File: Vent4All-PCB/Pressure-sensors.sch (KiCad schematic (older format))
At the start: 4 parts, among them U2 HSCMRRN100MDSA3, U3 HSCMRRN100MDSA3, U4 HSCMRRN100MDSA3, U5 HSCMRRN100MDSA3

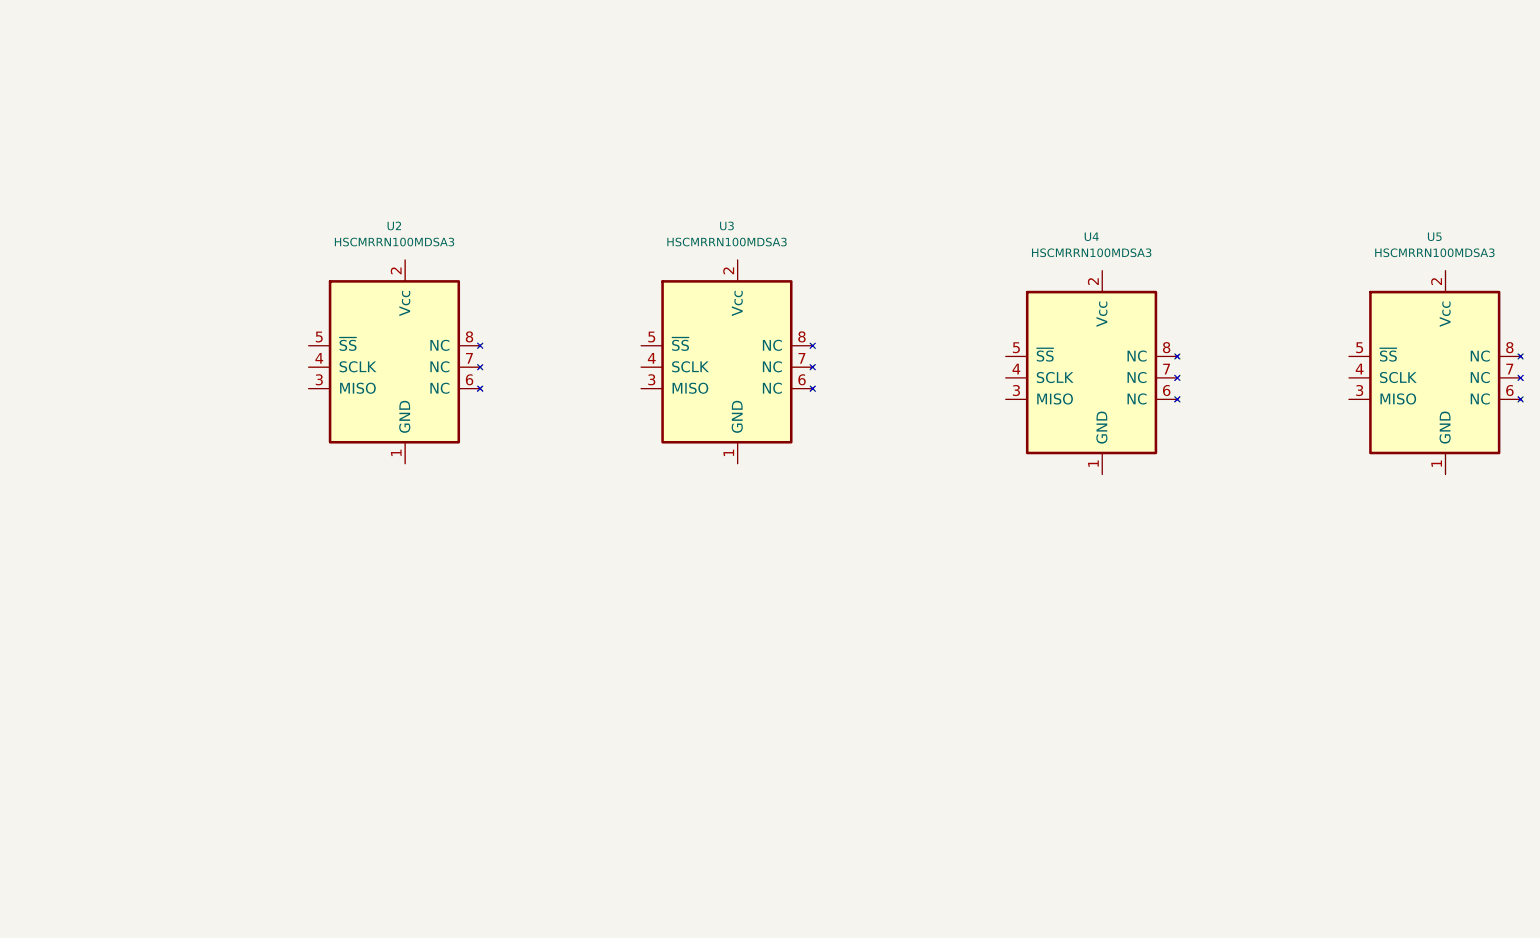
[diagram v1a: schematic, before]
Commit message: Added schematic connections for HSC sensors.
Note: this assumes HSC sensors will be soldered directly to the PCB. If we are placing them on daughter boards then we will need to choose the pin header connectors and move the HSC symbols into a separate sheet.
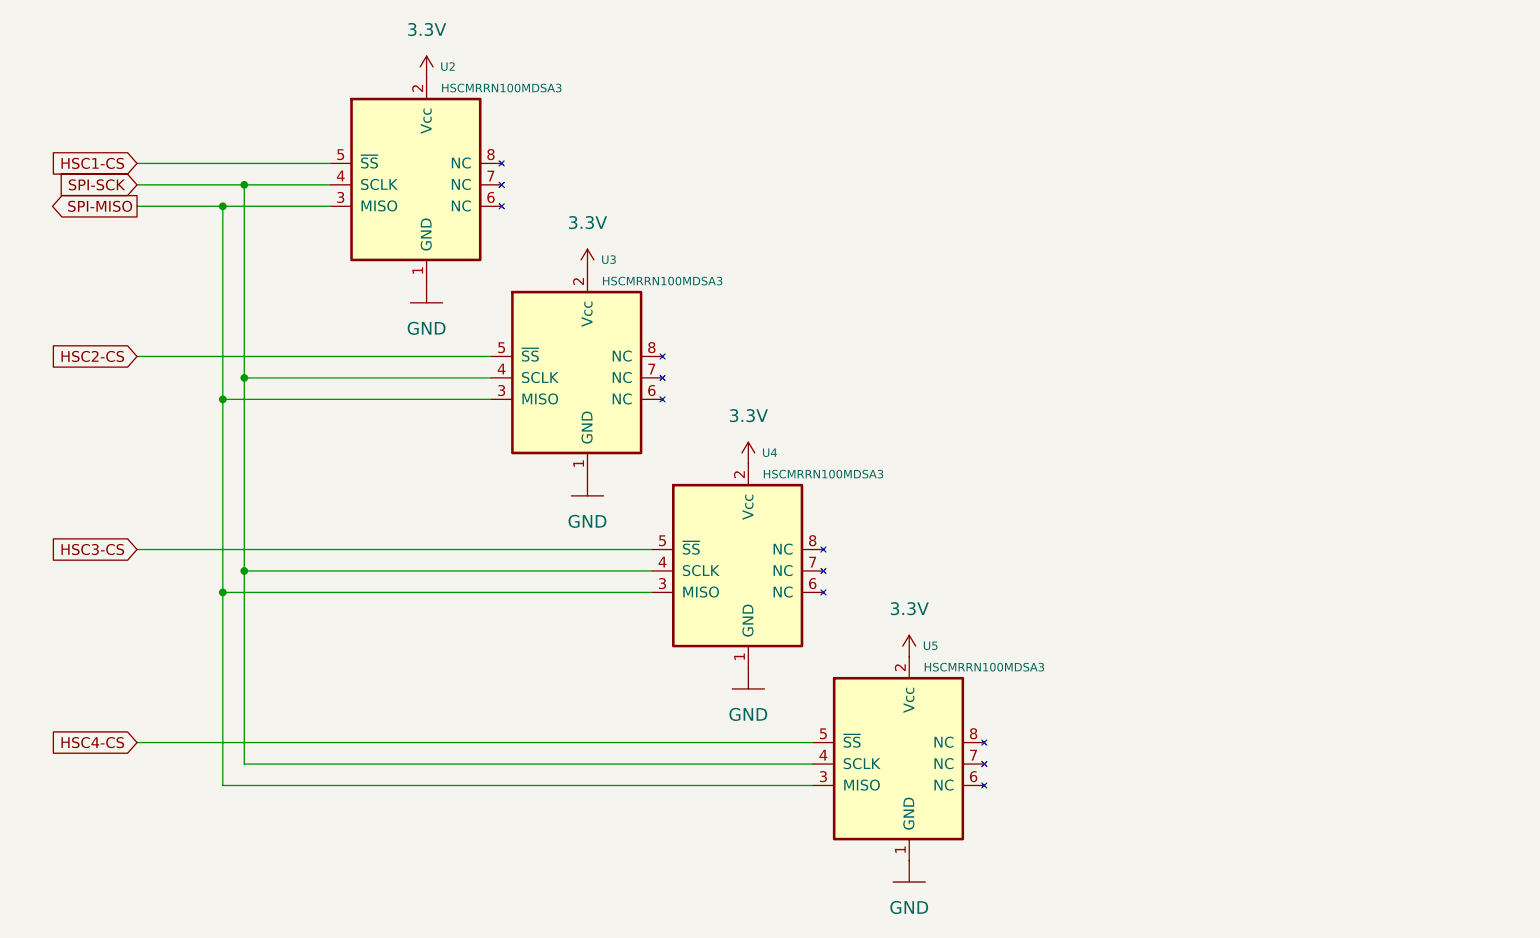
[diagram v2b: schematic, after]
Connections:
- net SPI-MISO: now reaches U2.3 (MISO)
- net SPI-MISO: now also U3.3 (MISO), U4.3 (MISO), U5.3 (MISO)
- net SPI-SCK: now reaches U2.4 (SCLK)
- net SPI-SCK: now also U3.4 (SCLK), U4.4 (SCLK), U5.4 (SCLK)
- net HSC1-CS: now reaches U2.5 (~SS)
- net HSC2-CS: now reaches U3.5 (~SS)
- net HSC3-CS: now reaches U4.5 (~SS)
- net HSC4-CS: now reaches U5.5 (~SS)
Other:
- moved on the sheet: U2, U3, U4, U5
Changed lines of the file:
@@
 $EndDescr
-$Comp
-L Vent4All_Library:HSCMRRN100MDSA3 U2
-U 1 1 5EBCB846
-P 2250 3250
-F 0 "U2" H 3200 4657 39  0000 C CNN
-F 1 "HSCMRRN100MDSA3" H 3200 4582 39  0000 C CNN
-F 2 "Vent4All:HSCMRRN100MDSA3_SOIC-8" H 2250 3250 39  0001 C CNN
-F 3 "https://www.mouser.com/datasheet/2/187/honeywell-sensing-trustability-hsc-series-high-acc-708740.pdf" H 2250 3250 39  0001 C CNN
-	1    2250 3250
-	1    0    0    -1
-$EndComp
 $Comp
 L Vent4All_Library:HSCMRRN100MDSA3 U3
 U 1 1 5EBCBFD8
-P 3800 3250
-F 0 "U3" H 4750 4657 39  0000 C CNN
-F 1 "HSCMRRN100MDSA3" H 4750 4582 39  0000 C CNN
-F 2 "Vent4All:HSCMRRN100MDSA3_SOIC-8" H 3800 3250 39  0001 C CNN
-F 3 "https://www.mouser.com/datasheet/2/187/honeywell-sensing-trustability-hsc-series-high-acc-708740.pdf" H 3800 3250 39  0001 C CNN
-	1    3800 3250
+P 3100 3300
+F 0 "U3" H 4200 4600 39  0000 C CNN
+F 1 "HSCMRRN100MDSA3" H 4450 4500 39  0000 C CNN
+F 2 "Vent4All:HSCMRRN100MDSA3_SOIC-8" H 3100 3300 39  0001 C CNN
+F 3 "https://www.mouser.com/datasheet/2/187/honeywell-sensing-trustability-hsc-series-high-acc-708740.pdf" H 3100 3300 39  0001 C CNN
+	1    3100 3300
 	1    0    0    -1
 $EndComp
@@
 L Vent4All_Library:HSCMRRN100MDSA3 U4
 U 1 1 5EBCC5F2
-P 5500 3300
-F 0 "U4" H 6450 4707 39  0000 C CNN
-F 1 "HSCMRRN100MDSA3" H 6450 4632 39  0000 C CNN
-F 2 "Vent4All:HSCMRRN100MDSA3_SOIC-8" H 5500 3300 39  0001 C CNN
-F 3 "https://www.mouser.com/datasheet/2/187/honeywell-sensing-trustability-hsc-series-high-acc-708740.pdf" H 5500 3300 39  0001 C CNN
-	1    5500 3300
+P 3850 4200
+F 0 "U4" H 4950 5500 39  0000 C CNN
+F 1 "HSCMRRN100MDSA3" H 5200 5400 39  0000 C CNN
+F 2 "Vent4All:HSCMRRN100MDSA3_SOIC-8" H 3850 4200 39  0001 C CNN
+F 3 "https://www.mouser.com/datasheet/2/187/honeywell-sensing-trustability-hsc-series-high-acc-708740.pdf" H 3850 4200 39  0001 C CNN
+	1    3850 4200
 	1    0    0    -1
 $EndComp
@@
 L Vent4All_Library:HSCMRRN100MDSA3 U5
 U 1 1 5EBCC9C1
-P 7100 3300
-F 0 "U5" H 8050 4707 39  0000 C CNN
-F 1 "HSCMRRN100MDSA3" H 8050 4632 39  0000 C CNN
-F 2 "Vent4All:HSCMRRN100MDSA3_SOIC-8" H 7100 3300 39  0001 C CNN
-F 3 "https://www.mouser.com/datasheet/2/187/honeywell-sensing-trustability-hsc-series-high-acc-708740.pdf" H 7100 3300 39  0001 C CNN
-	1    7100 3300
+P 4600 5100
+F 0 "U5" H 5700 6400 39  0000 C CNN
+F 1 "HSCMRRN100MDSA3" H 5950 6300 39  0000 C CNN
+F 2 "Vent4All:HSCMRRN100MDSA3_SOIC-8" H 4600 5100 39  0001 C CNN
+F 3 "https://www.mouser.com/datasheet/2/187/honeywell-sensing-trustability-hsc-series-high-acc-708740.pdf" H 4600 5100 39  0001 C CNN
+	1    4600 5100
 	1    0    0    -1
 $EndComp
+$Comp
+L Vent4All_Library:HSCMRRN100MDSA3 U2
+U 1 1 5EBCB846
+P 2350 2400
+F 0 "U2" H 3450 3700 39  0000 C CNN
+F 1 "HSCMRRN100MDSA3" H 3700 3600 39  0000 C CNN
+F 2 "Vent4All:HSCMRRN100MDSA3_SOIC-8" H 2350 2400 39  0001 C CNN
+F 3 "https://www.mouser.com/datasheet/2/187/honeywell-sensing-trustability-hsc-series-high-acc-708740.pdf" H 2350 2400 39  0001 C CNN
+	1    2350 2400
+	1    0    0    -1
+$EndComp
+Wire Wire Line
+	2500 1650 2900 1650
+Text GLabel 2000 1650 0    50   Input ~ 0
+SPI-SCK
+Text GLabel 2000 1750 0    50   Output ~ 0
+SPI-MISO
+Wire Wire Line
+	2400 1750 2900 1750
+$Comp
+L Vent4All_Library:GND #GND?
+U 1 1 5EB9C3A4
+P 3350 2200
+F 0 "#GND?" H 3350 2200 50  0001 C CNN
+F 1 "GND" H 3350 2079 59  0000 C CNN
+F 2 "" H 3350 2200 50  0001 C CNN
+F 3 "" H 3350 2200 50  0001 C CNN
+	1    3350 2200
+	1    0    0    -1
+$EndComp
+Wire Wire Line
+	2500 1650 2500 2550
+Wire Wire Line
+	2400 1750 2400 2650
+Wire Wire Line
+	3650 2550 2500 2550
+Wire Wire Line
+	3650 2650 2400 2650
+$Comp
+L Vent4All_Library:GND #GND?
+U 1 1 5EB9F183
+P 4100 3100
+F 0 "#GND?" H 4100 3100 50  0001 C CNN
+F 1 "GND" H 4100 2979 59  0000 C CNN
+F 2 "" H 4100 3100 50  0001 C CNN
+F 3 "" H 4100 3100 50  0001 C CNN
+	1    4100 3100
+	1    0    0    -1
+$EndComp
+Connection ~ 2500 2550
+Wire Wire Line
+	2500 2550 2500 3450
+Connection ~ 2400 2650
+Wire Wire Line
+	2400 2650 2400 3550
+Wire Wire Line
+	4400 3450 2500 3450
+Wire Wire Line
+	4400 3550 2400 3550
+Wire Wire Line
+	2500 3450 2500 4350
+Wire Wire Line
+	2500 4350 5150 4350
+Connection ~ 2500 3450
+Wire Wire Line
+	2400 3550 2400 4450
+Wire Wire Line
+	2400 4450 5150 4450
+Connection ~ 2400 3550
+$Comp
+L Vent4All_Library:3.3V #SUPPLY?
+U 1 1 5EBA5B20
+P 3350 1150
+F 0 "#SUPPLY?" H 3350 1150 50  0001 C CNN
+F 1 "3.3V" H 3350 1372 59  0000 C CNN
+F 2 "" H 3350 1150 50  0001 C CNN
+F 3 "" H 3350 1150 50  0001 C CNN
+	1    3350 1150
+	1    0    0    -1
+$EndComp
+$Comp
+L Vent4All_Library:3.3V #SUPPLY?
+U 1 1 5EBA63D4
+P 4100 2050
+F 0 "#SUPPLY?" H 4100 2050 50  0001 C CNN
+F 1 "3.3V" H 4100 2272 59  0000 C CNN
+F 2 "" H 4100 2050 50  0001 C CNN
+F 3 "" H 4100 2050 50  0001 C CNN
+	1    4100 2050
+	1    0    0    -1
+$EndComp
+$Comp
+L Vent4All_Library:3.3V #SUPPLY?
+U 1 1 5EBA6694
+P 4850 2950
+F 0 "#SUPPLY?" H 4850 2950 50  0001 C CNN
+F 1 "3.3V" H 4850 3172 59  0000 C CNN
+F 2 "" H 4850 2950 50  0001 C CNN
+F 3 "" H 4850 2950 50  0001 C CNN
+	1    4850 2950
+	1    0    0    -1
+$EndComp
+$Comp
+L Vent4All_Library:3.3V #SUPPLY?
+U 1 1 5EBA6D0D
+P 5600 3850
+F 0 "#SUPPLY?" H 5600 3850 50  0001 C CNN
+F 1 "3.3V" H 5600 4072 59  0000 C CNN
+F 2 "" H 5600 3850 50  0001 C CNN
+F 3 "" H 5600 3850 50  0001 C CNN
+	1    5600 3850
+	1    0    0    -1
+$EndComp
+Text GLabel 2000 1550 0    50   Input ~ 0
+HSC1-CS
+Text GLabel 2000 2450 0    50   Input ~ 0
+HSC2-CS
+Wire Wire Line
+	2000 1650 2500 1650
+Connection ~ 2500 1650
+Wire Wire Line
+	2000 1750 2400 1750
+Connection ~ 2400 1750
+Wire Wire Line
+	2000 1550 2900 1550
+Wire Wire Line
+	2000 2450 3650 2450
+Text GLabel 2000 3350 0    50   Input ~ 0
+HSC3-CS
+Text GLabel 2000 4250 0    50   Input ~ 0
+HSC4-CS
+Wire Wire Line
+	2000 4250 5150 4250
+Wire Wire Line
+	2000 3350 4400 3350
+$Comp
+L Vent4All_Library:GND #GND?
+U 1 1 5EBA97AE
+P 4850 4000
+F 0 "#GND?" H 4850 4000 50  0001 C CNN
+F 1 "GND" H 4850 3879 59  0000 C CNN
+F 2 "" H 4850 4000 50  0001 C CNN
+F 3 "" H 4850 4000 50  0001 C CNN
+	1    4850 4000
+	1    0    0    -1
+$EndComp
+$Comp
+L Vent4All_Library:GND #GND?
+U 1 1 5EBA9B96
+P 5600 4900
+F 0 "#GND?" H 5600 4900 50  0001 C CNN
+F 1 "GND" H 5600 4779 59  0000 C CNN
+F 2 "" H 5600 4900 50  0001 C CNN
+F 3 "" H 5600 4900 50  0001 C CNN
+	1    5600 4900
+	1    0    0    -1
+$EndComp
